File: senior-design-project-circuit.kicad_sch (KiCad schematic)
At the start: 49 parts, among them J1 Micro_SD_Card, J10 Conn_01x01_Male, J11 Conn_01x01_Male, J12 Conn_01x01_Male, J15 Conn_01x01_Male, J2A1 Conn_01x15_Female, J2B1 Conn_01x15_Female, J3 Conn_01x16_Male, J4 USB_B_Micro, J5 Conn_01x02, J6 Conn_01x06_Female, J7 Conn_01x01_Male, J8 Conn_01x01_Male, J9 Conn_01x01_Male, SW1 SW_Push, SW2 SW_Push, SW3 SW_Push, U1 4050, U2 LM2594M-3.3, U3 MCP73831-2-OT

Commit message: Add files via upload
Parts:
- added C3, C4: 1u, Capacitor_SMD:C_0603_1608Metric_Pad1.08x0.95mm_HandSolder, symbol Device:C
- added SW?: SW_SPDT, symbol Switch:SW_SPDT
- added U4: NCP164-ASN330, Package_TO_SOT_SMD:SOT-23-5, symbol Battery_Management:MCP73831-2-OT
- C1, C2: value 10p -> 10u
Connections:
- net +3V3: now also SW?.2 (B); no longer C2.1, COUT1.1, J5.1 (Pin_1), J7.1 (Pin_1), L1.2, U2.4 (FB), U3.3 (VBAT)
- net GNDREF: now also C3.2, C4.2, U4.2 (GND)
- net Net-(J3-Pad15): now reaches J3.15 (Pin_15)
- new net: COUT1.1, L1.2, SW?.3 (C), U2.4 (FB)
- new net: C2.1, C4.1, J5.1 (Pin_1), J7.1 (Pin_1), U3.3 (VBAT), U4.1 (EN), U4.3 (Vin)
- new net: C3.1, SW?.1 (A), U4.5 (Vout)
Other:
- moved on the sheet: C1, C2, CIN1, COUT1, D1, J15, J3, J4, J5, J7, JP1, JP2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

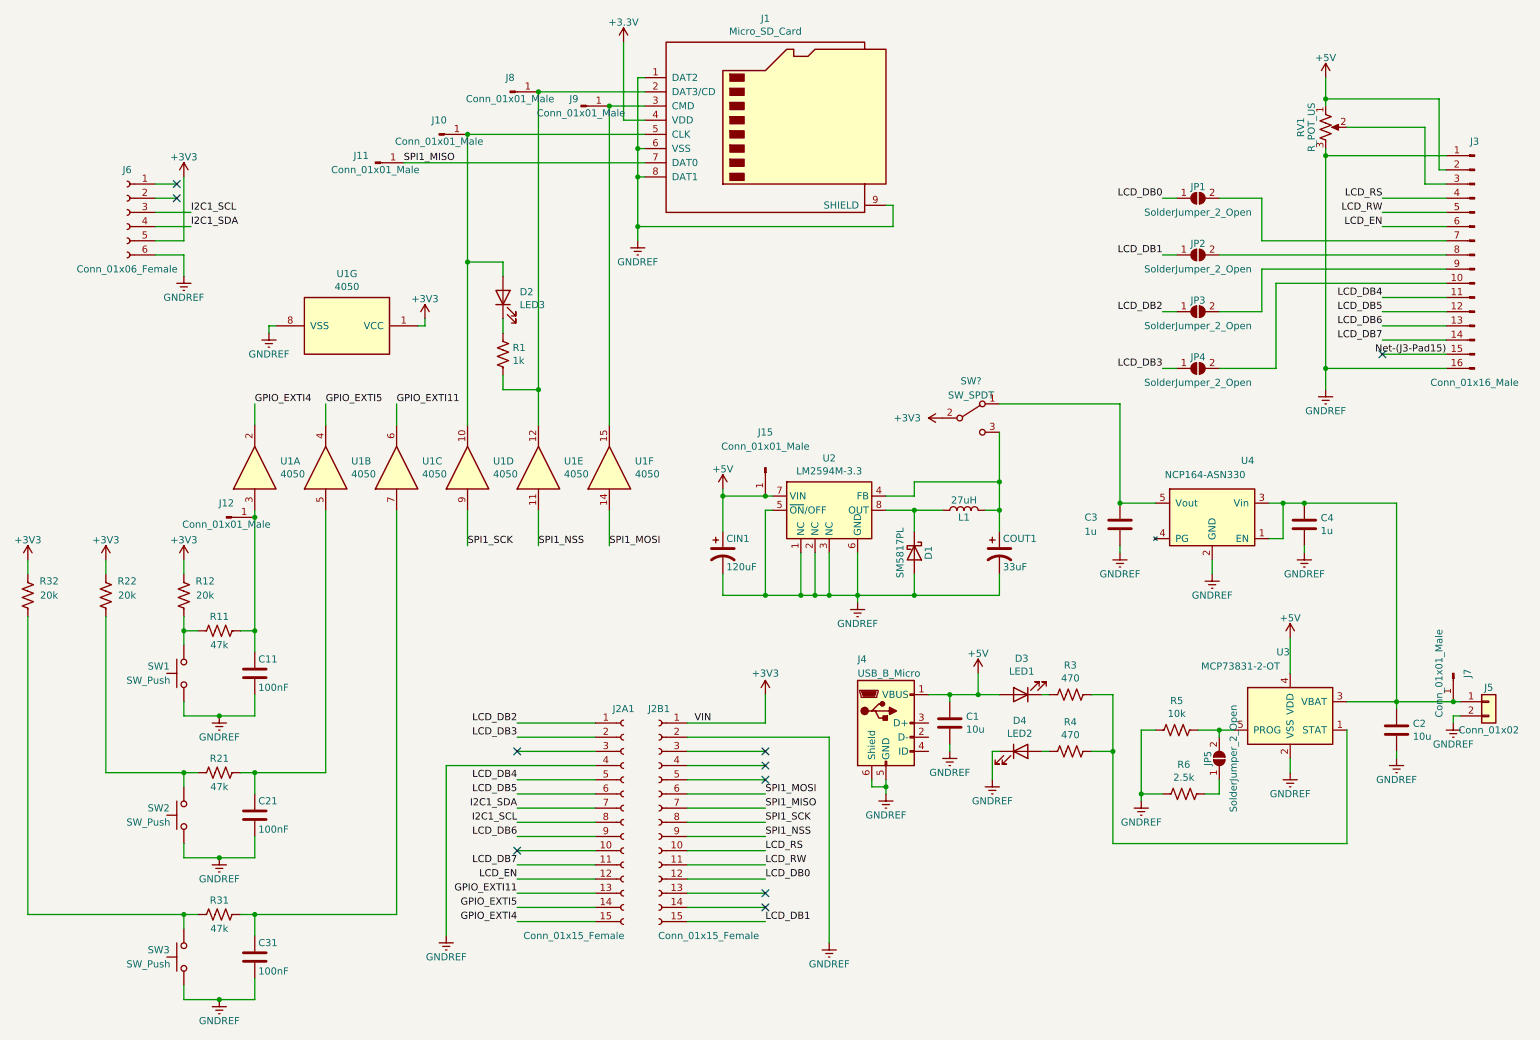
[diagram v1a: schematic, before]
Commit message: Added labels to schematic pin headers
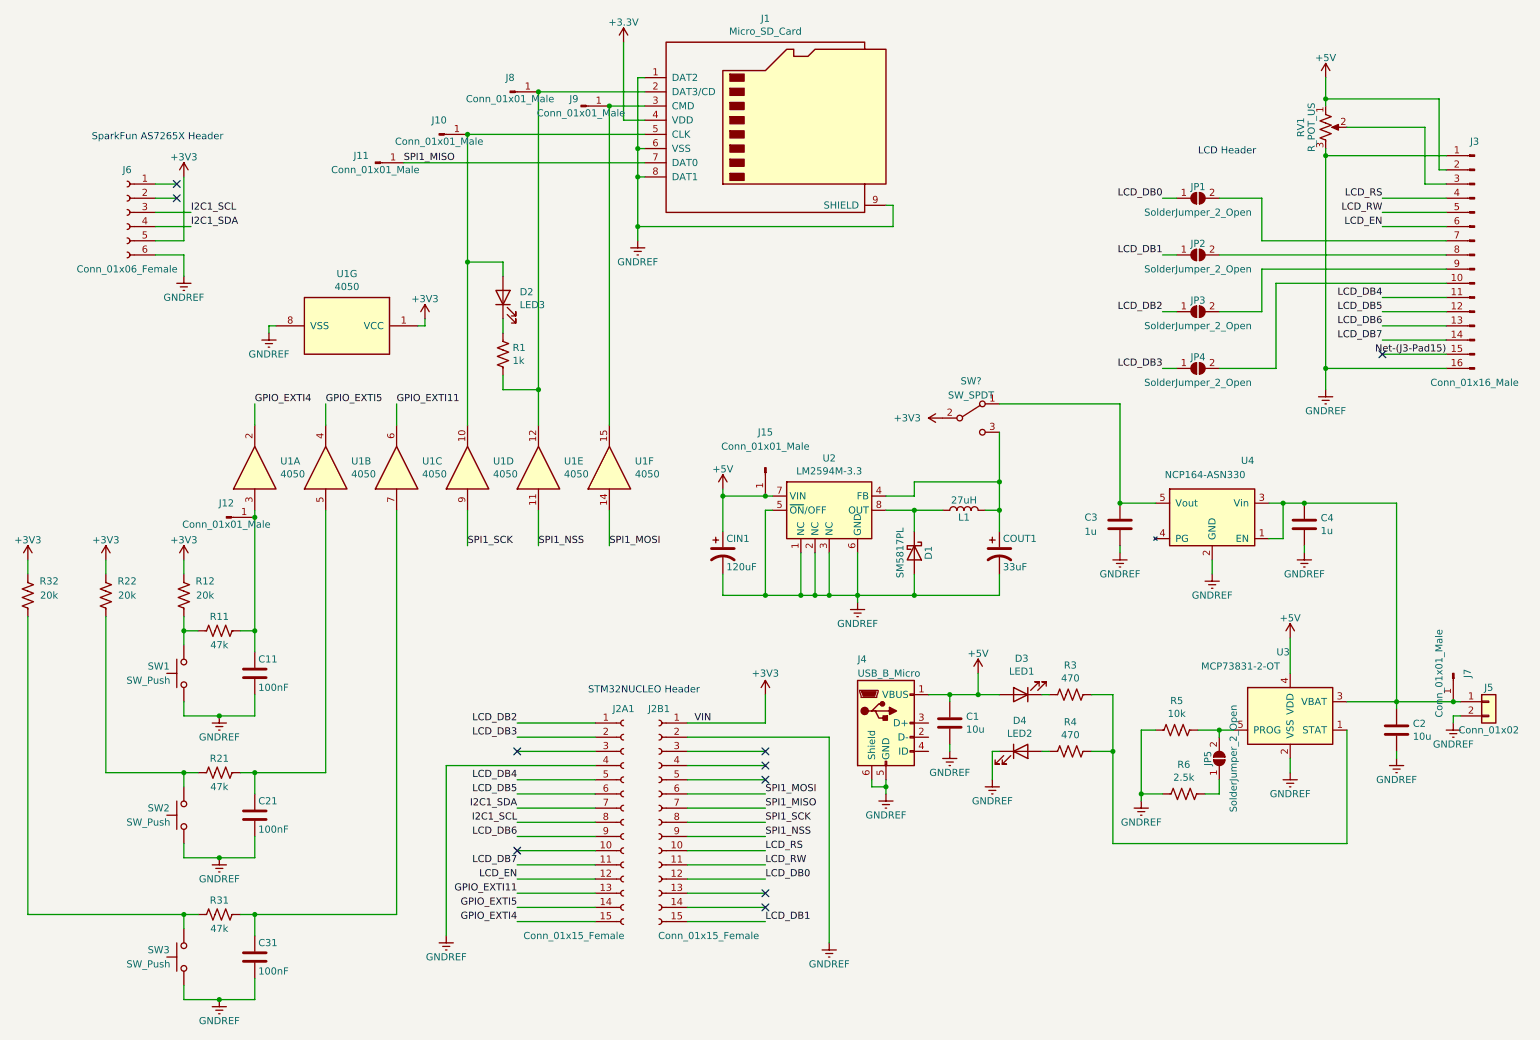
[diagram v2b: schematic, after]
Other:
- note added: "LCD Header"
- note added: "STM32NUCLEO Header"
- note added: "SparkFun AS7265X Header"
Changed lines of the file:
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@@
     (rev "1")
     (comment 1 "Authors: Emily Currie and Abe Jordan")
-    (comment 2 "MicroSD SPI layout taken from Adafruit")
   )
   (junction (at 186.69 134.62) (diameter 0) (color 0 0 0 0)
@@
     (stroke (width 0) (type default) (color 0 0 0 0))
   )
+  (text "STM32NUCLEO Header" (at 116.84 134.62 0)
+    (effects (font (size 1.27 1.27)) (justify left bottom))
+  )
+  (text "SparkFun AS7265X Header" (at 27.94 35.56 0)
+    (effects (font (size 1.27 1.27)) (justify left bottom))
+  )
+  (text "LCD Header" (at 226.06 38.1 0)
+    (effects (font (size 1.27 1.27)) (justify left bottom))
+  )
   (label "LCD_DB3" (at 219.71 76.2 180)
